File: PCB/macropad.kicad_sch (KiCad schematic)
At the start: 23 parts, among them SW1 RotaryEncoder_Switch, SW10 SW_Push, SW11 SW_Push, SW2 RotaryEncoder_Switch, SW3 SW_Push, SW4 SW_Push, SW5 SW_Push, SW6 SW_Push, SW7 SW_Push, SW8 SW_Push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

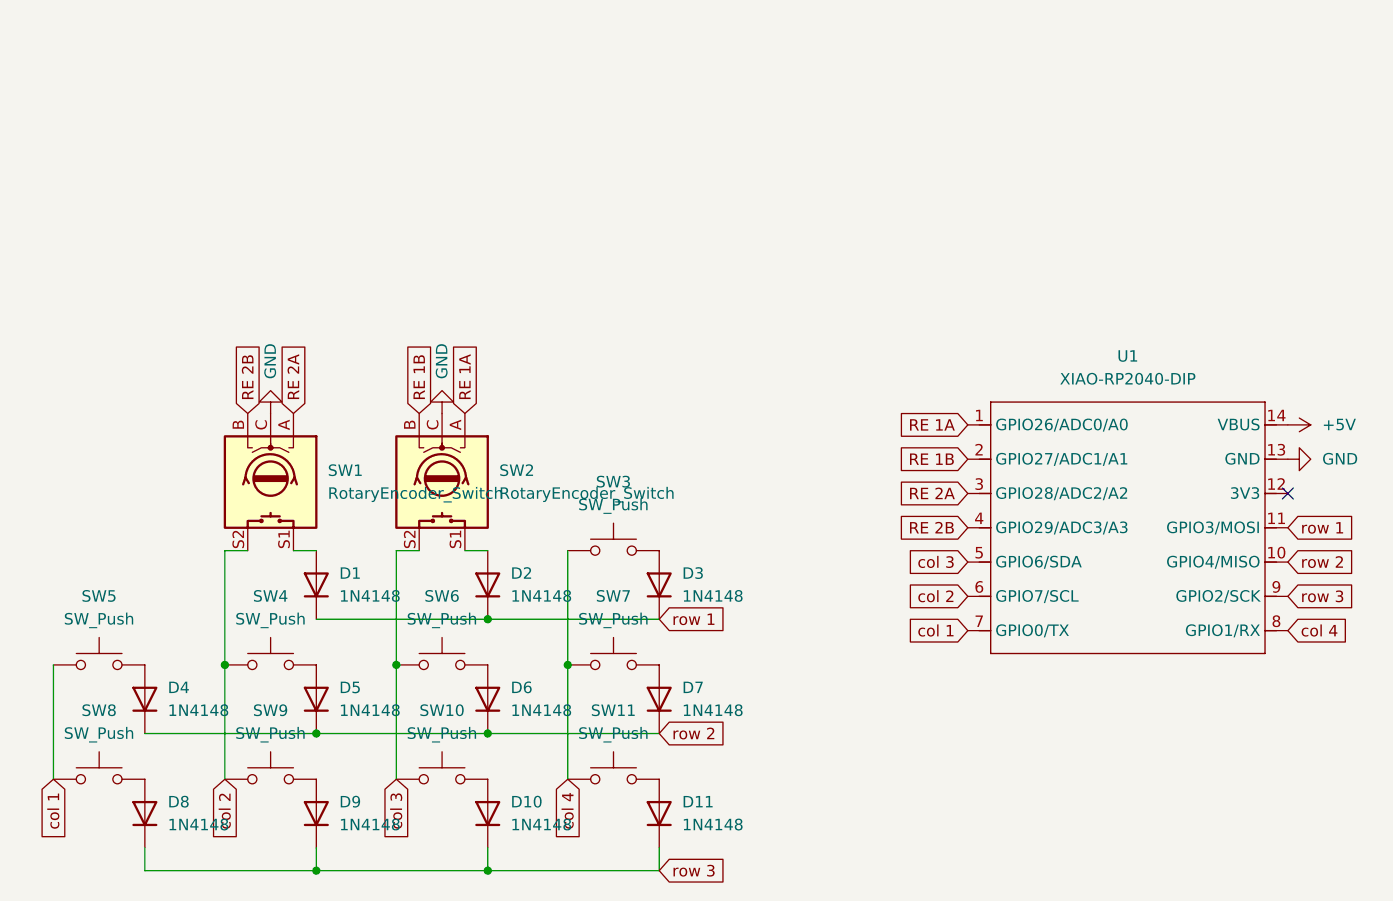
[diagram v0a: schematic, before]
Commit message: Fixed ground fill on the PCB
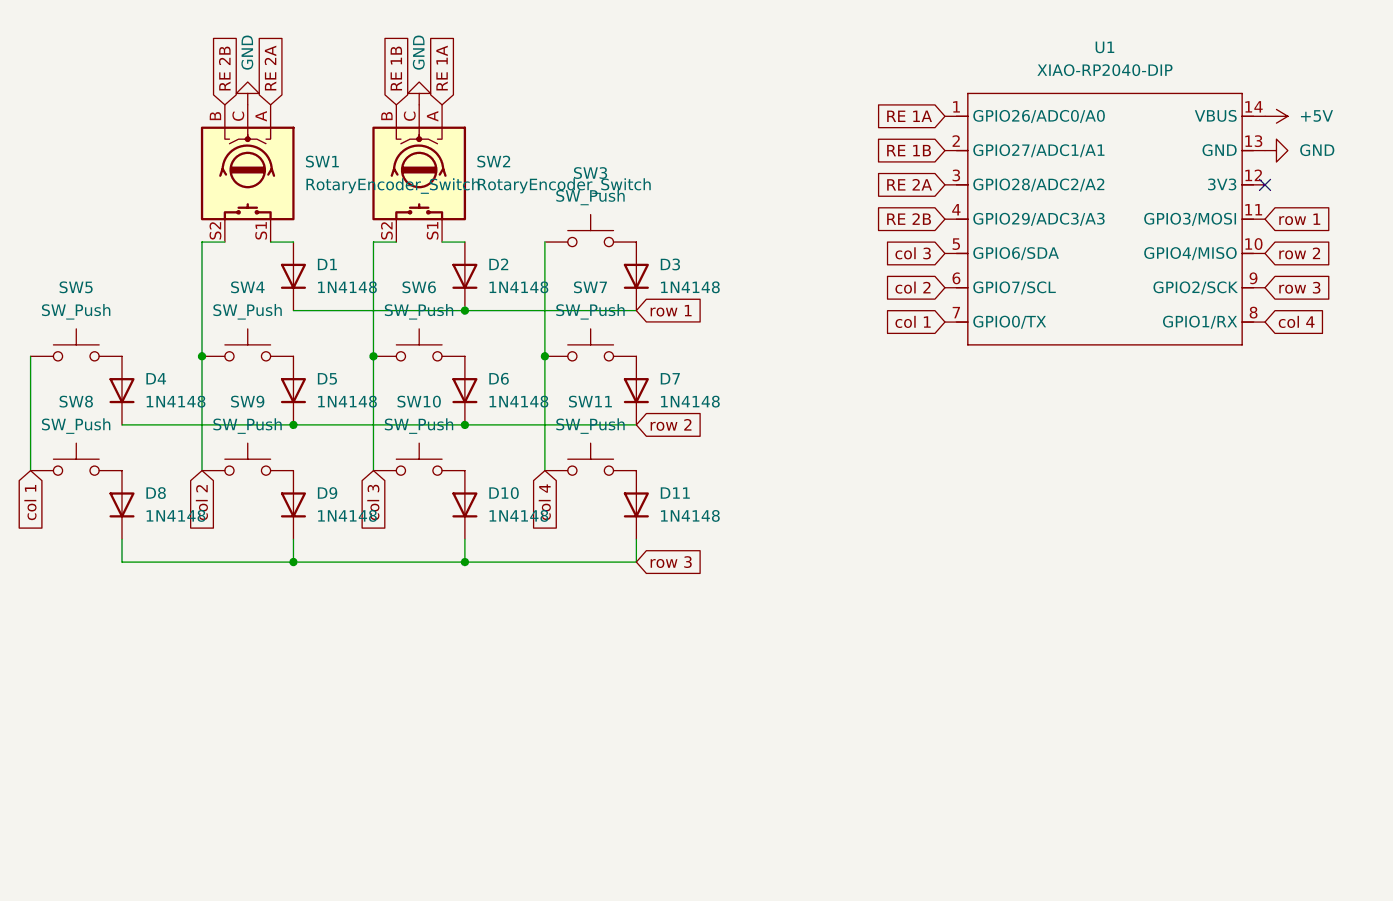
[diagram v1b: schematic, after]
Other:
- title: (none) -> nikitabr0's hackpad
- moved on the sheet: D1, D10, D11, D2, D3, D4, D5, D6, D7, D8, D9, SW1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
